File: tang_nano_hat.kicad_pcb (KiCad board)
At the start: 2 copper layers, 70 x 26 mm, 2 parts, among them J1 Conn_01x24, J2 Conn_01x24

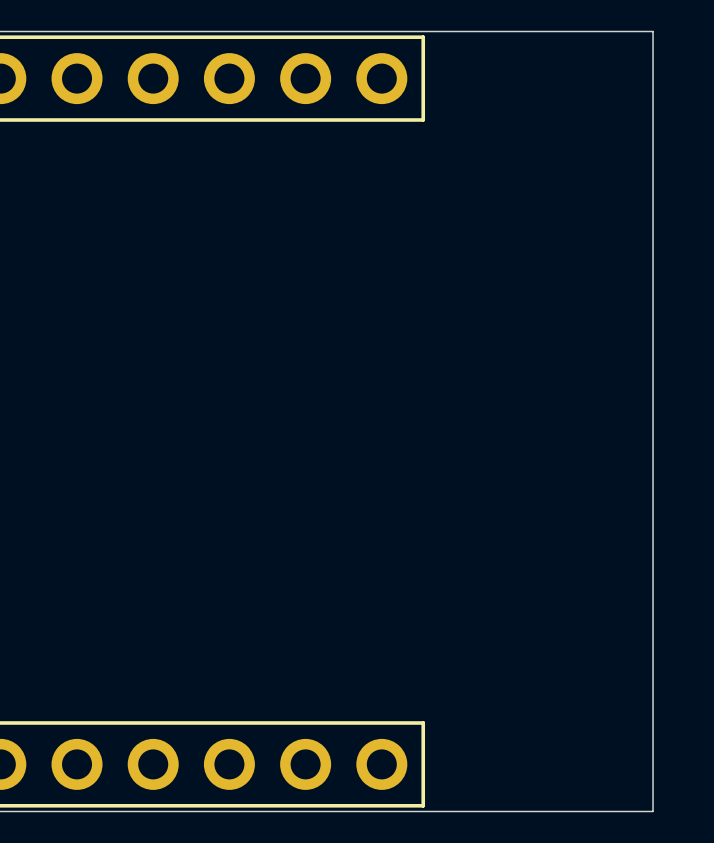
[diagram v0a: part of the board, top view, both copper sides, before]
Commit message: feat: VBUS sensing schematic
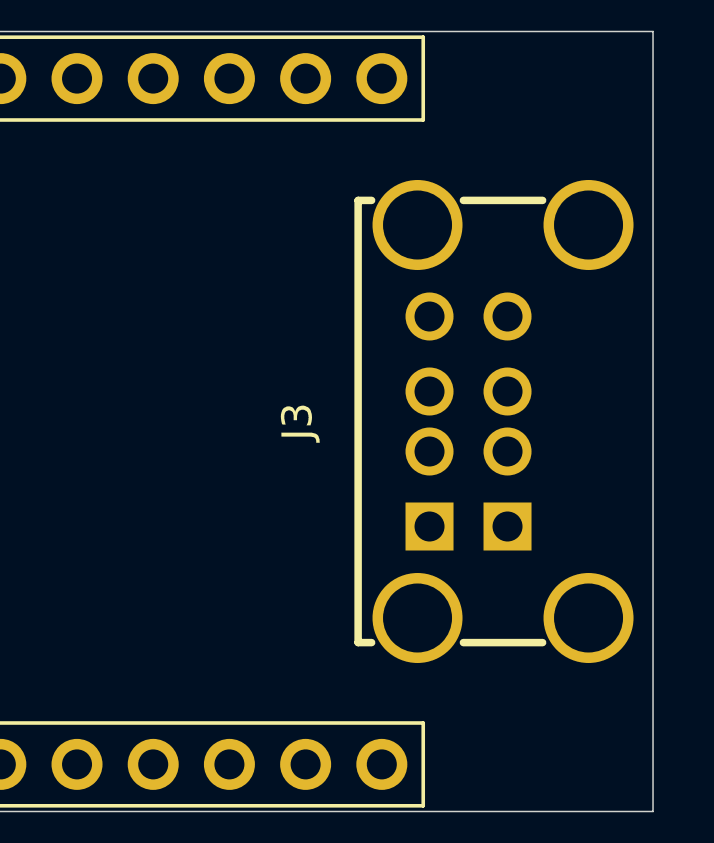
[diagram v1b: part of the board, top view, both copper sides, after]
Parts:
- added J3: AF SS-JB17.6, C456021:USB-A-TH_AF-SS-JB17.6, F.Cu at (165.0, 63.0)

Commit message: feat: basic func
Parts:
- added C1: 10nF, Capacitor_SMD:C_0603_1608Metric, F.Cu at (147.6, 68.8)
- added C2: 1uF, Capacitor_SMD:C_0805_2012Metric, F.Cu at (145.8, 58.8)
- added C3: 100nF, Capacitor_SMD:C_0603_1608Metric, F.Cu at (145.9, 60.5)
- added C4: 1nF, Capacitor_SMD:C_1206_3216Metric, F.Cu at (150.6, 57.9)
- added D1: D_Zener, Diode_SMD:D_SOD-523, F.Cu at (149.8, 68.0)
- added R1: 100K, Resistor_SMD:R_0603_1608Metric, F.Cu at (147.6, 67.3)
- added R2: 1K, Resistor_SMD:R_0603_1608Metric, F.Cu at (144.6, 67.3)
- added R3: 150K, Resistor_SMD:R_0603_1608Metric, F.Cu at (147.6, 70.3)
- added R4: 33, Resistor_SMD:R_0603_1608Metric, F.Cu at (143.3, 64.0)
- added R5: 33, Resistor_SMD:R_0603_1608Metric, F.Cu at (143.3, 62.0)
- added R6: 100, Resistor_SMD:R_0603_1608Metric, F.Cu at (150.2, 64.2)
- added R7: 100, Resistor_SMD:R_0603_1608Metric, F.Cu at (150.1, 61.8)
- added R8: 1M, Resistor_SMD:R_0603_1608Metric, F.Cu at (148.7, 57.1)
- added TP1: DM_RX, TestPoint:TestPoint_Pad_D1.0mm, F.Cu at (140.7, 64.0)
- added TP2: DP_RX, TestPoint:TestPoint_Pad_D1.0mm, F.Cu at (137.9, 62.1)
- added U1: SN74LVC2G17DBVR, C10429:SOT-23-6_L2.9-W1.6-P0.95-LS2.8-BL, F.Cu at (146.9, 63.0)
- added U2: TPD2EUSB30ADRTR, C94934:SOT-9X3-3_L1.0-W0.8-P0.35-LS1.0-BR, F.Cu at (151.2, 63.0)
- moved J3 8.10 mm to (156.9, 63.0)
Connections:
- J1 pad 1: unconnected-(J1-Pin_1-Pad1) -> /63
- J1 pad 10: unconnected-(J1-Pin_10-Pad10) -> /77
- J1 pad 11: unconnected-(J1-Pin_11-Pad11) -> /76
- J1 pad 12: unconnected-(J1-Pin_12-Pad12) -> /75
- J1 pad 13: unconnected-(J1-Pin_13-Pad13) -> /74
- J1 pad 14: unconnected-(J1-Pin_14-Pad14) -> /73
- J1 pad 15: unconnected-(J1-Pin_15-Pad15) -> /72
- J1 pad 16: unconnected-(J1-Pin_16-Pad16) -> /71
- J1 pad 17: unconnected-(J1-Pin_17-Pad17) -> /70
- J1 pad 18: unconnected-(J1-Pin_18-Pad18) -> /5V
- J1 pad 19: unconnected-(J1-Pin_19-Pad19) -> /48
- J1 pad 2: unconnected-(J1-Pin_2-Pad2) -> /86
- J1 pad 20: unconnected-(J1-Pin_20-Pad20) -> /49
- J1 pad 21: unconnected-(J1-Pin_21-Pad21) -> /31
- J1 pad 22: unconnected-(J1-Pin_22-Pad22) -> /32
- J1 pad 23: unconnected-(J1-Pin_23-Pad23) -> GND
- J1 pad 24: unconnected-(J1-Pin_24-Pad24) -> 3V3
- J1 pad 3: unconnected-(J1-Pin_3-Pad3) -> /85
- J1 pad 4: unconnected-(J1-Pin_4-Pad4) -> /84
- J1 pad 5: unconnected-(J1-Pin_5-Pad5) -> /83
- J1 pad 6: unconnected-(J1-Pin_6-Pad6) -> /82
- J1 pad 7: unconnected-(J1-Pin_7-Pad7) -> /81
- J1 pad 8: unconnected-(J1-Pin_8-Pad8) -> /80
- J1 pad 9: unconnected-(J1-Pin_9-Pad9) -> /79
- J2 pad 1: unconnected-(J2-Pin_1-Pad1) -> /38
- J2 pad 10: unconnected-(J2-Pin_10-Pad10) -> /30
- J2 pad 11: unconnected-(J2-Pin_11-Pad11) -> /33
- J2 pad 12: unconnected-(J2-Pin_12-Pad12) -> /34
- J2 pad 13: unconnected-(J2-Pin_13-Pad13) -> /40
- J2 pad 14: unconnected-(J2-Pin_14-Pad14) -> /35
- J2 pad 15: unconnected-(J2-Pin_15-Pad15) -> /41
- J2 pad 16: unconnected-(J2-Pin_16-Pad16) -> /42
- J2 pad 17: unconnected-(J2-Pin_17-Pad17) -> /51
- J2 pad 18: unconnected-(J2-Pin_18-Pad18) -> /53
- J2 pad 19: unconnected-(J2-Pin_19-Pad19) -> /54
- J2 pad 2: unconnected-(J2-Pin_2-Pad2) -> /37
- J2 pad 20: unconnected-(J2-Pin_20-Pad20) -> /55
- J2 pad 21: unconnected-(J2-Pin_21-Pad21) -> /56
- J2 pad 22: unconnected-(J2-Pin_22-Pad22) -> /57
- J2 pad 23: unconnected-(J2-Pin_23-Pad23) -> /68
- J2 pad 24: unconnected-(J2-Pin_24-Pad24) -> /69
- J2 pad 3: unconnected-(J2-Pin_3-Pad3) -> /36
- J2 pad 4: unconnected-(J2-Pin_4-Pad4) -> /39
- J2 pad 5: unconnected-(J2-Pin_5-Pad5) -> /25
- J2 pad 6: unconnected-(J2-Pin_6-Pad6) -> /26
- J2 pad 7: unconnected-(J2-Pin_7-Pad7) -> /27
- J2 pad 8: unconnected-(J2-Pin_8-Pad8) -> /28
- J2 pad 9: unconnected-(J2-Pin_9-Pad9) -> /29
- J3 pad 1: unconnected-(J3-VCC-Pad1) -> VBUS
- J3 pad 10: unconnected-(J3-SHELL-Pad10) -> Net-(C4-Pad1)
- J3 pad 11: unconnected-(J3-SHELL-Pad11) -> Net-(C4-Pad1)
- J3 pad 12: unconnected-(J3-SHELL-Pad12) -> Net-(C4-Pad1)
- J3 pad 2: unconnected-(J3-D--Pad2) -> /D-
- J3 pad 3: unconnected-(J3-D+-Pad3) -> /D+
- J3 pad 4: unconnected-(J3-GND-Pad4) -> GND
- J3 pad 5: unconnected-(J3-VCC-Pad5) -> VBUS
- J3 pad 6: unconnected-(J3-D--Pad6) -> /D-
- J3 pad 7: unconnected-(J3-D+-Pad7) -> /D+
- J3 pad 8: unconnected-(J3-GND-Pad8) -> GND
- J3 pad 9: unconnected-(J3-SHELL-Pad9) -> Net-(C4-Pad1)
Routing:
- net /25: track 0.00 -> 35.0 mm
- net /26: track 0.00 -> 31.6 mm
- net Net-(C4-Pad1): track 0.00 -> 30.0 mm, vias 0 -> 1
- net /27: track 0.00 -> 28.9 mm
- net 3V3: track 0.00 -> 25.7 mm
- net VBUS: track 0.00 -> 8.93 mm
- net /D-: track 0.00 -> 7.70 mm
- net /D+: track 0.00 -> 7.66 mm
- net Net-(C1-Pad1): track 0.00 -> 4.41 mm
- net Net-(U1-1A): track 0.00 -> 1.71 mm
- net Net-(U1-2A): track 0.00 -> 1.71 mm
- net Net-(U1-2Y): track 0.00 -> 1.57 mm
- net Net-(U1-1Y): track 0.00 -> 1.57 mm
- net GND: vias 0 -> 66
- added copper zone on B.Cu, net GND
- added copper zone on F.Cu, net GND
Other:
- board text added: "25"
- board text added: "26"
- board text added: "27"
- board text added: "28"
- board text added: "29"
- board text added: "30"
- board text added: "31"
- board text added: "32"
- board text added: "33"
- board text added: "34"
- board text added: "35"
- board text added: "36"
- board text added: "37"
- board text added: "38"
- board text added: "39"
- board text added: "3V3"
- board text added: "40"
- board text added: "41"
- board text added: "42"
- board text added: "48"
- board text added: "49"
- board text added: "51"
- board text added: "53"
- board text added: "54"
- board text added: "55"
- board text added: "56"
- board text added: "57"
- board text added: "5V"
- board text added: "63"
- board text added: "68"
- board text added: "69"
- board text added: "70"
- board text added: "71"
- board text added: "72"
- board text added: "73"
- board text added: "74"
- board text added: "75"
- board text added: "76"
- board text added: "77"
- board text added: "79"
- board text added: "80"
- board text added: "81"
- board text added: "82"
- board text added: "83"
- board text added: "84"
- board text added: "85"
- board text added: "86"
- board text added: "GND"

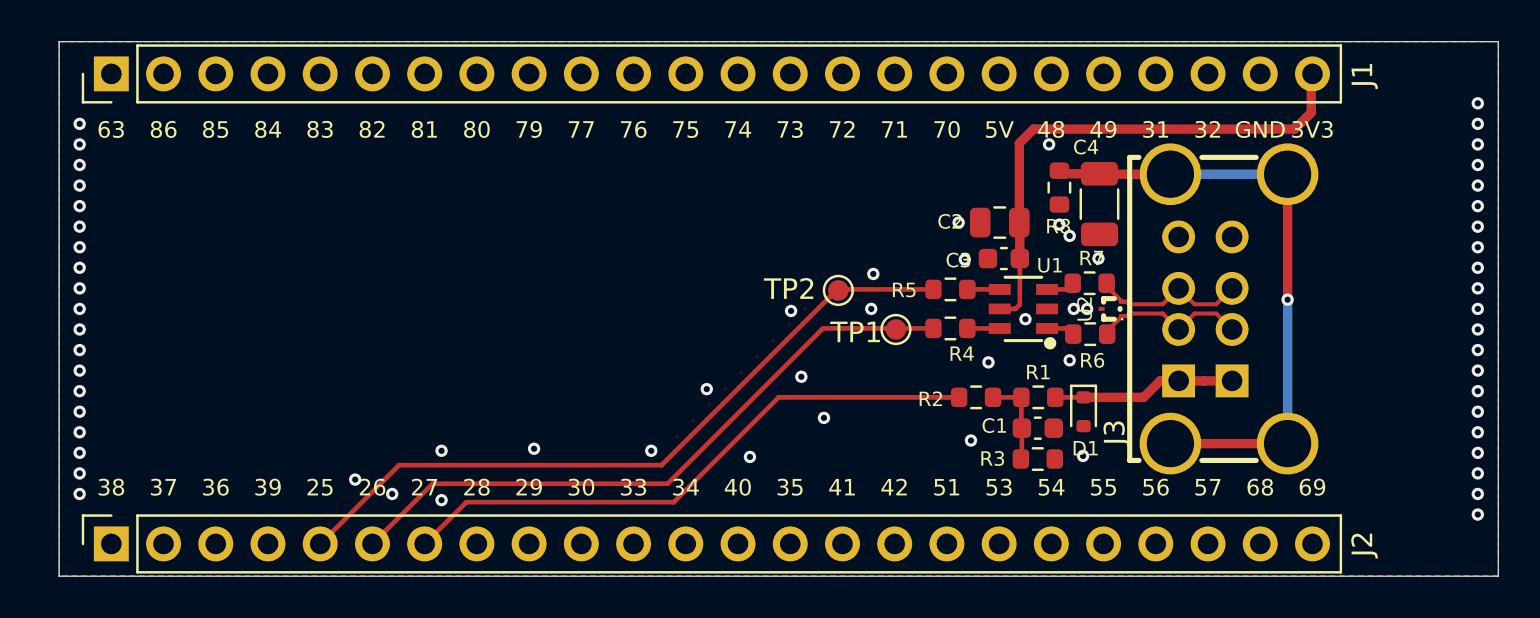
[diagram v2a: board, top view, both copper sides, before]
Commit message: feat: vbus switch and case
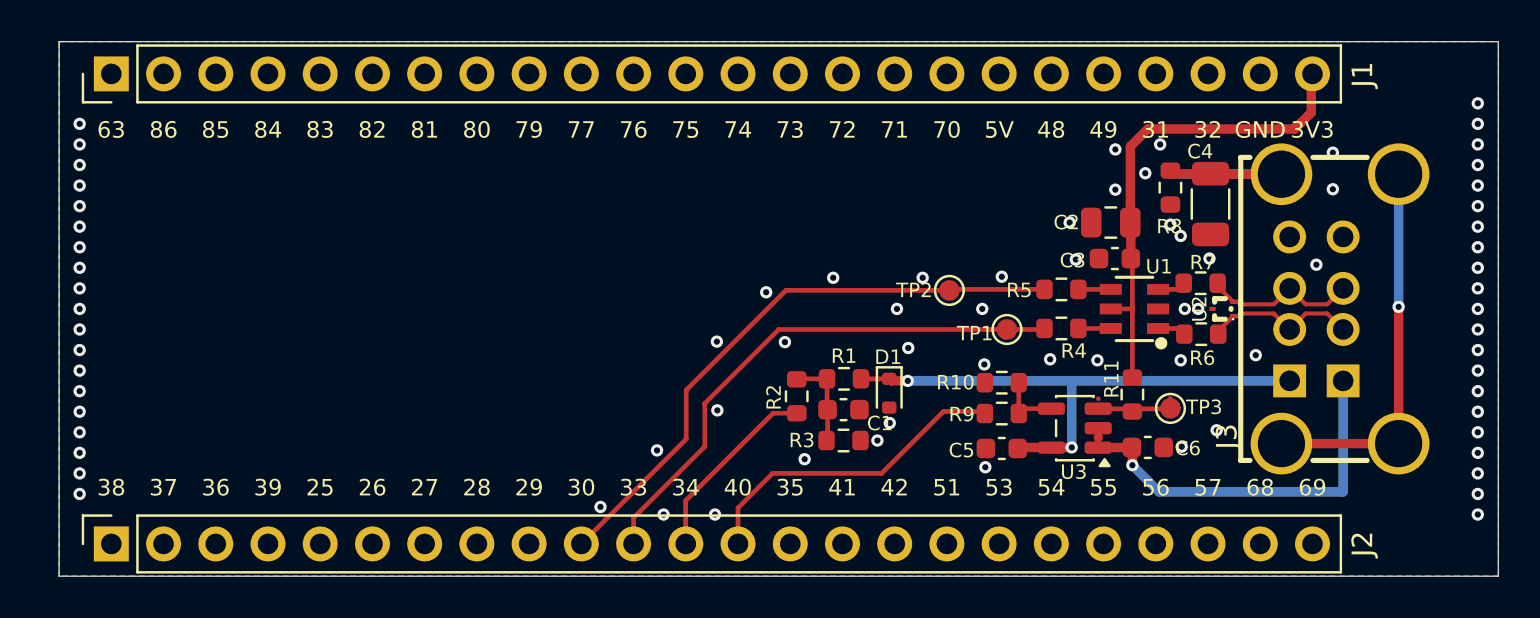
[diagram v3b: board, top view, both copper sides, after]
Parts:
- added C5: 100nF, Capacitor_SMD:C_0603_1608Metric, F.Cu at (145.8, 69.8)
- added C6: 100nF, Capacitor_SMD:C_0603_1608Metric, F.Cu at (152.9, 69.7)
- added R10: 100K, Resistor_SMD:R_0603_1608Metric, F.Cu at (145.8, 66.6)
- added R11: 10K, Resistor_SMD:R_0603_1608Metric, F.Cu at (152.2, 67.2)
- added R9: 1K, Resistor_SMD:R_0603_1608Metric, F.Cu at (145.8, 68.1)
- added TP3: DP_RXVBUS_FAULT_N, TestPoint:TestPoint_Pad_D1.0mm, F.Cu at (154.1, 67.8)
- added U3: AP2151DWG-7, Package_TO_SOT_SMD:SOT-23-5, F.Cu at (149.4, 68.8)
- moved D1 9.49 mm to (140.4, 67.1)
- moved C1 9.49 mm to (138.2, 67.9)
- moved R1 9.49 mm to (138.2, 66.4)
- moved R3 9.49 mm to (138.2, 69.4)
- moved R2 8.73 mm to (135.9, 67.2), turned to -90 degrees
- moved C2 5.40 mm to (151.2, 58.8)
- moved C3 5.40 mm to (151.3, 60.5)
- moved C4 5.40 mm to (156.0, 57.9)
- moved J3 5.40 mm to (162.3, 63.0)
- moved R4 5.40 mm to (148.8, 64.0)
- moved R5 5.40 mm to (148.8, 62.0)
- moved R6 5.40 mm to (155.6, 64.2)
- moved R7 5.40 mm to (155.5, 61.8)
- moved R8 5.40 mm to (154.1, 57.1)
- moved TP1 5.40 mm to (146.1, 64.0)
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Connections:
- D1 pad 1: VBUS -> HOST_VBUS
- J3 pad 1: VBUS -> HOST_VBUS
- J3 pad 5: VBUS -> KEYBOARD_VBUS
- R1 pad 1: VBUS -> HOST_VBUS
- R2 pad 2: /27 -> /34
- R4 pad 2: /26 -> /33
- R5 pad 2: /25 -> /30
- TP1 pad 1: /26 -> /33
- TP2 pad 1: /25 -> /30
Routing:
- net /25: track 35.0 -> 0.00 mm
- net /26: track 31.6 -> 0.00 mm
- net /30: track 0.00 -> 29.1 mm
- net /27: track 28.9 -> 0.00 mm
- net HOST_VBUS: track 0.00 -> 26.6 mm, vias 0 -> 2
- net /33: track 0.00 -> 26.3 mm
- net KEYBOARD_VBUS: track 0.00 -> 18.7 mm, vias 0 -> 1
- net /40: track 0.00 -> 15.9 mm
- net /34: track 0.00 -> 9.39 mm
- net VBUS: track 8.93 -> 0.00 mm
- net Net-(U3-~{FLT}): track 0.00 -> 3.53 mm
- net Net-(U3-EN): track 0.00 -> 2.95 mm
- net 3V3: track 25.7 -> 23.7 mm
- net GND: vias 66 -> 79
